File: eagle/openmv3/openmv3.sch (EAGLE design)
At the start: 56 parts, among them Q1 MOSFET, U1 STM32F765VGT6, U2 OV7725, U3 BD33IA, X1 47571-0001

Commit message: Added 3 more I/O pins
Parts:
- added R4: 100K, sfe:RESISTOR0603-RES
- JP3: device pinhead:PINHD-1X5 -> SparkFun-Connectors:M06SILK_FEMALE_PTH
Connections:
- net N$1 renamed VREFH
- net N$10 renamed LED_IR_4
- net N$12 renamed VDDA
- net N$13 renamed AVDD
- net N$14 renamed LED_IR_3
- net N$15 renamed DVDD
- net N$17 renamed LED_IR_5
- net N$2 renamed OSC_OUT
- net N$3 renamed VREFN
- net N$4 renamed OSC_IN
- net N$5 renamed LED_IR_2
- net N$6 renamed LED_B_2
- net N$7 renamed VBUS_PRE
- net N$8 renamed LED_R_2
- net N$9 renamed LED_G_2
- removed net EXPST: U1.PD8/FSMC_D13/USART3_TX
- removed net FREX: U1.PD9/FSMC_D14/USART3_RX
- removed net TIM4_CH3: JP1.4, U1.PD14/FSMC_D0/TIM4_CH3
- new net ADC: JP1.2, U1.PA7/SPI1_MOSI/TIM8_CH1N/TIM14_CH1TIM3_CH2
- new net CAN_RX: JP1.4, U1.PB3/JTDO/TRACESWO/SPI3_SCK/I2S3_CK/TIM2_CH2/SPI1_SCK
- new net CAN_TX: JP1.3, U1.PB4/NJTRST/SPI3_MISO/TIM3_CH1/SPI1_MISO/I2S3EXT_SD
- net BOOT0: now also JP3.4; no longer JP1.2
- net FSIN: now also JP1.1, U1.PD3/FSMC_CLK/USART2_CTS; no longer JP1.3
- net GND: now also JP3.1, R4.1; no longer JP3.5
- net NRST: no longer JP1.1
- net SWCLK: now also JP3.6; no longer JP3.1
- net SWDIO: now also JP3.5; no longer JP3.2
- net VBUS: now also R4.2
- net VCC: now also JP3.2; no longer JP3.4

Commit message: Swap BOOT0 and RST pins
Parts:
- R4: value 100K -> 470K
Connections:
- net BOOT0: now also JP3.3, RN5A.2; no longer JP3.4, RN5B.2
- net GND: now also RN5A.1; no longer RN5B.1
- net NRST: now also JP3.4, RN5B.2; no longer JP3.3, RN5A.2
- net VCC: now also RN5B.1; no longer RN5A.1
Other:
- note added: "Copyright (c) 2016 Ibrahim Abd Elkader <i.abdalkader@gmail.com>"
- note removed: "Copyright (c) 2013 Ibrahim Abd Elkader <i.abdalkader@gmail.com>"
- moved on the sheet: RN5A, RN5B
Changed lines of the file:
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@@
 <part name="P+13" library="mux" deviceset="VCC" device=""/>
 <part name="JP3" library="SparkFun-Connectors" deviceset="M06" device="SILK_FEMALE_PTH"/>
-<part name="R4" library="sfe" deviceset="RESISTOR" device="0603-RES" value="100K"/>
+<part name="R4" library="sfe" deviceset="RESISTOR" device="0603-RES" value="470K"/>
 <part name="GND7" library="supply1" deviceset="GND" device=""/>
 <part name="VBUS1" library="iofault" deviceset="VBUS" device=""/>
@@
 <wire x1="-20.32" y1="-48.26" x2="-20.32" y2="335.28" width="0.1524" layer="94"/>
 <wire x1="254" y1="335.28" x2="254" y2="-48.26" width="0.1524" layer="94"/>
-<text x="-15.24" y="-30.48" size="3.81" layer="150">Copyright (c) 2013 Ibrahim Abd Elkader &lt;i.abdalkader@gmail.com&gt;</text>
+<text x="-15.24" y="-30.48" size="3.81" layer="150">Copyright (c) 2016 Ibrahim Abd Elkader &lt;i.abdalkader@gmail.com&gt;</text>
 <text x="-15.24" y="-35.56" size="3.81" layer="150">This work is licensed under the Creative Commons Attribution-ShareAlike 3.0 License.</text>
 <text x="-15.24" y="-40.64" size="3.81" layer="150">To view a copy of this license, visit http://creativecommons.org/licenses/by-sa/3.0/</text>
@@
 <attribute name="NAME" x="374.015" y="187.452" size="1.016" layer="95"/>
 </instance>
-<instance part="RN5" gate="A" x="50.8" y="205.74" smashed="yes" rot="R270">
+<instance part="RN5" gate="B" x="50.8" y="205.74" smashed="yes" rot="R270">
 <attribute name="VALUE" x="47.752" y="203.2" size="1.778" layer="96" rot="R270"/>
 <attribute name="NAME" x="50.292" y="207.645" size="1.016" layer="95" rot="R270"/>
 </instance>
-<instance part="RN5" gate="B" x="22.86" y="154.94" smashed="yes" rot="R90">
+<instance part="RN5" gate="A" x="22.86" y="154.94" smashed="yes" rot="R90">
 <attribute name="VALUE" x="25.908" y="157.48" size="1.778" layer="96" rot="R90"/>
 <attribute name="NAME" x="23.368" y="153.035" size="1.016" layer="95" rot="R90"/>
@@
 <segment>
 <pinref part="GND45" gate="1" pin="GND"/>
-<pinref part="RN5" gate="B" pin="1"/>
+<pinref part="RN5" gate="A" pin="1"/>
 <wire x1="22.86" y1="149.86" x2="22.86" y2="132.08" width="0.1524" layer="91"/>
 </segment>
@@
 <label x="53.34" y="165.1" size="1.778" layer="95"/>
 <pinref part="U1" gate="G$1" pin="NRST"/>
-<pinref part="RN5" gate="A" pin="2"/>
+<pinref part="RN5" gate="B" pin="2"/>
 <wire x1="50.8" y1="165.1" x2="50.8" y2="200.66" width="0.1524" layer="91"/>
 </segment>
 <segment>
-<label x="396.24" y="256.54" size="1.778" layer="95"/>
-<pinref part="JP3" gate="G$1" pin="3"/>
-<wire x1="396.24" y1="256.54" x2="406.4" y2="256.54" width="0.1524" layer="91"/>
+<pinref part="JP3" gate="G$1" pin="4"/>
+<wire x1="406.4" y1="259.08" x2="396.24" y2="259.08" width="0.1524" layer="91"/>
+<label x="396.24" y="259.08" size="1.778" layer="95"/>
 </segment>
 </net>
@@
 <label x="53.34" y="162.56" size="1.778" layer="95"/>
 <pinref part="U1" gate="G$1" pin="BOOT0"/>
-<pinref part="RN5" gate="B" pin="2"/>
+<pinref part="RN5" gate="A" pin="2"/>
 <wire x1="22.86" y1="162.56" x2="22.86" y2="160.02" width="0.1524" layer="91"/>
 </segment>
 <segment>
-<pinref part="JP3" gate="G$1" pin="4"/>
-<wire x1="406.4" y1="259.08" x2="396.24" y2="259.08" width="0.1524" layer="91"/>
-<label x="396.24" y="259.08" size="1.778" layer="95"/>
+<pinref part="JP3" gate="G$1" pin="3"/>
+<wire x1="406.4" y1="256.54" x2="396.24" y2="256.54" width="0.1524" layer="91"/>
+<label x="396.24" y="256.54" size="1.778" layer="95"/>
 </segment>
 </net>
@@
 <segment>
 <pinref part="P+2" gate="VCC" pin="VCC"/>
-<pinref part="RN5" gate="A" pin="1"/>
+<pinref part="RN5" gate="B" pin="1"/>
 <wire x1="50.8" y1="210.82" x2="50.8" y2="220.98" width="0.1524" layer="91"/>
 </segment>

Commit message: Update OpenMV3 design files.
* Fix silk screen.
* Fix power diode part number.
* Replace IR LEDs.
* Revert last two commits.
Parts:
- removed R4: 470K, sfe:RESISTOR0603-RES
- D1: value BAT54C -> PMEG2005CT
- JP3: device SparkFun-Connectors:M06SILK_FEMALE_PTH -> pinhead:PINHD-1X5
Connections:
- net AVDD renamed N$13
- net DVDD renamed N$15
- net LED_B_2 renamed N$6
- net LED_G_2 renamed N$9
- net LED_IR_2 renamed N$5
- net LED_IR_3 renamed N$14
- net LED_IR_4 renamed N$10
- net LED_IR_5 renamed N$17
- net LED_R_2 renamed N$8
- net OSC_IN renamed N$4
- net OSC_OUT renamed N$2
- net VBUS_PRE renamed N$7
- net VDDA renamed N$12
- net VREFH renamed N$1
- net VREFN renamed N$3
- removed net ADC: JP1.2, U1.PA7/SPI1_MOSI/TIM8_CH1N/TIM14_CH1TIM3_CH2
- removed net CAN_RX: JP1.4, U1.PB3/JTDO/TRACESWO/SPI3_SCK/I2S3_CK/TIM2_CH2/SPI1_SCK
- removed net CAN_TX: JP1.3, U1.PB4/NJTRST/SPI3_MISO/TIM3_CH1/SPI1_MISO/I2S3EXT_SD
- new net EXPST: U1.PD8/FSMC_D13/USART3_TX
- new net FREX: U1.PD9/FSMC_D14/USART3_RX
- new net TIM4_CH3: JP1.4, U1.PD14/FSMC_D0/TIM4_CH3
- net BOOT0: now also JP1.2, RN5B.2; no longer JP3.3, RN5A.2
- net FSIN: now also JP1.3; no longer JP1.1, U1.PD3/FSMC_CLK/USART2_CTS
- net GND: now also JP3.5, RN5B.1; no longer JP3.1, R4.1, RN5A.1
- net NRST: now also JP1.1, JP3.3, RN5A.2; no longer JP3.4, RN5B.2
- net SWCLK: now also JP3.1; no longer JP3.6
- net SWDIO: now also JP3.2; no longer JP3.5
- net VBUS: no longer R4.2
- net VCC: now also JP3.4, RN5A.1; no longer JP3.2, RN5B.1
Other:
- note added: "Copyright (c) 2013 Ibrahim Abd Elkader <i.abdalkader@gmail.com>"
- note removed: "Copyright (c) 2016 Ibrahim Abd Elkader <i.abdalkader@gmail.com>"
- moved on the sheet: RN5A, RN5B

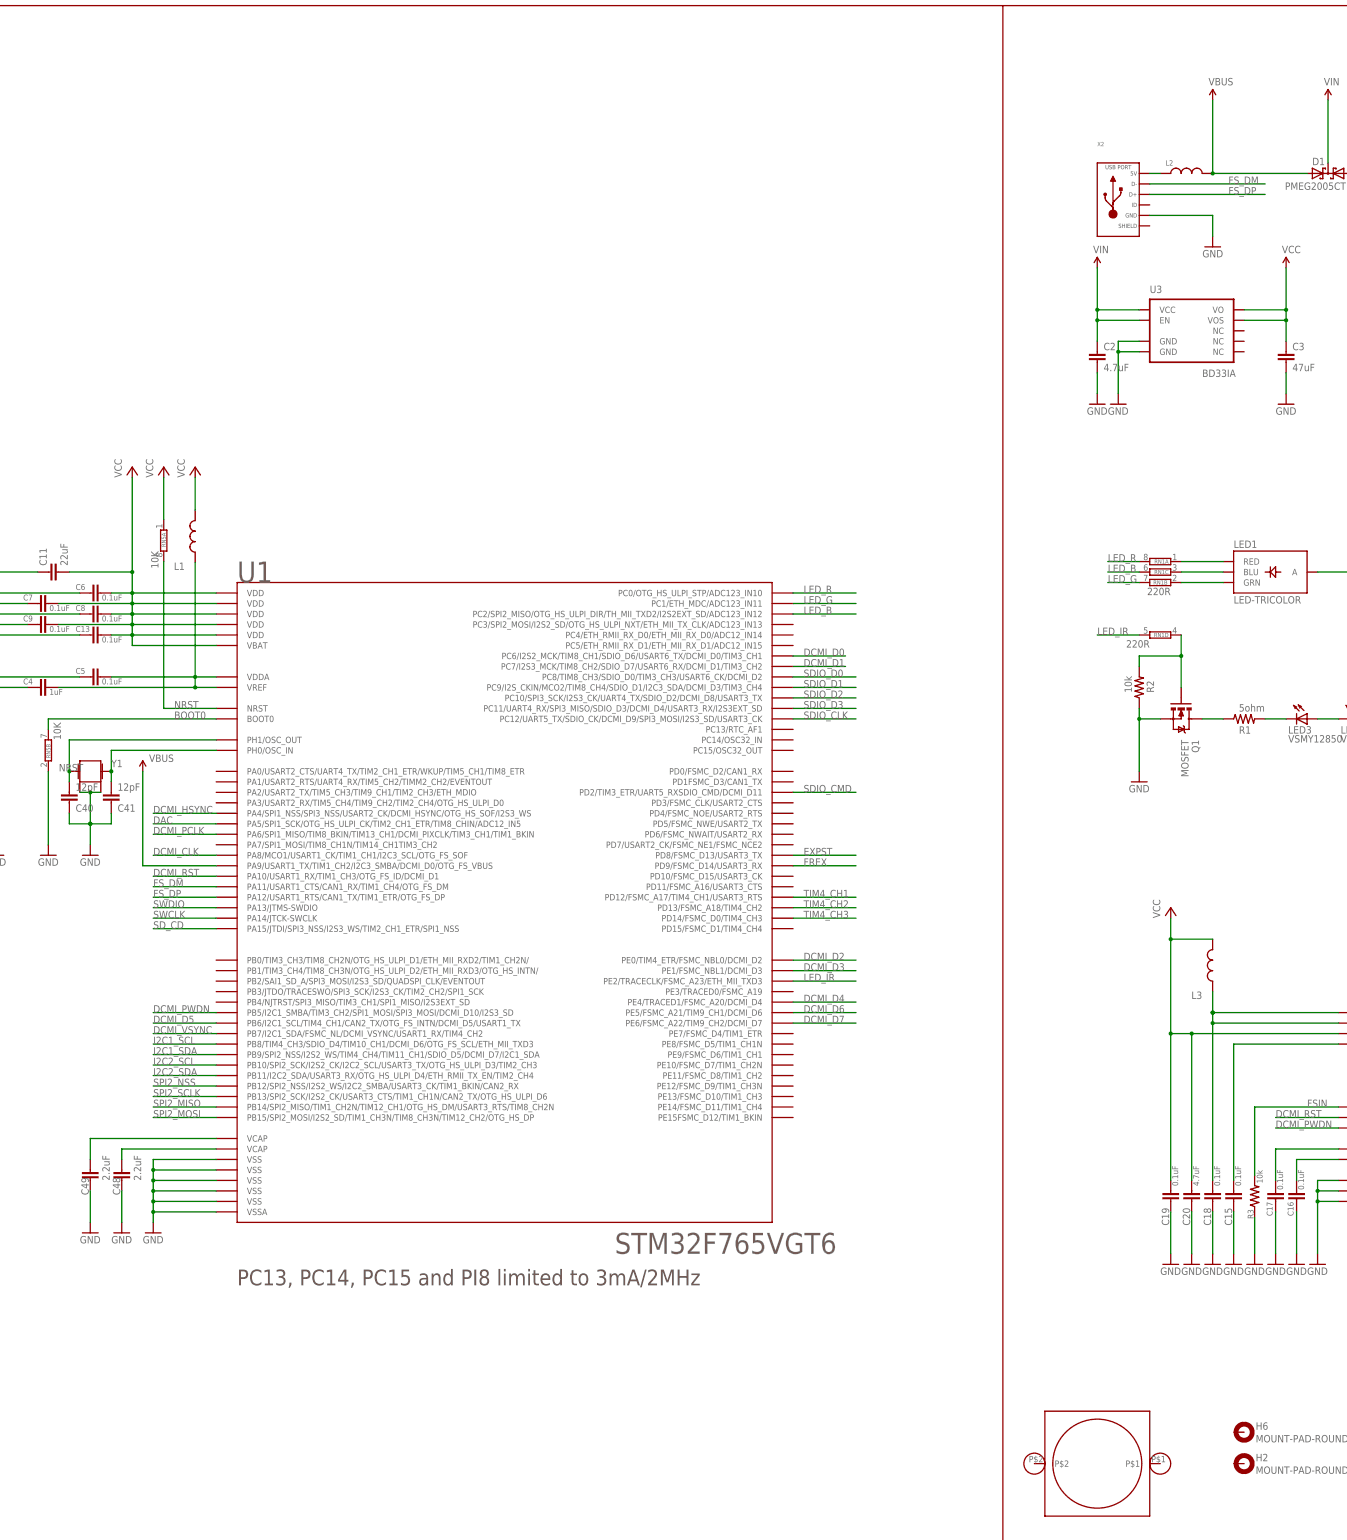
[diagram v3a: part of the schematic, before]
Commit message: Add missing parts values to OMV3 design files.
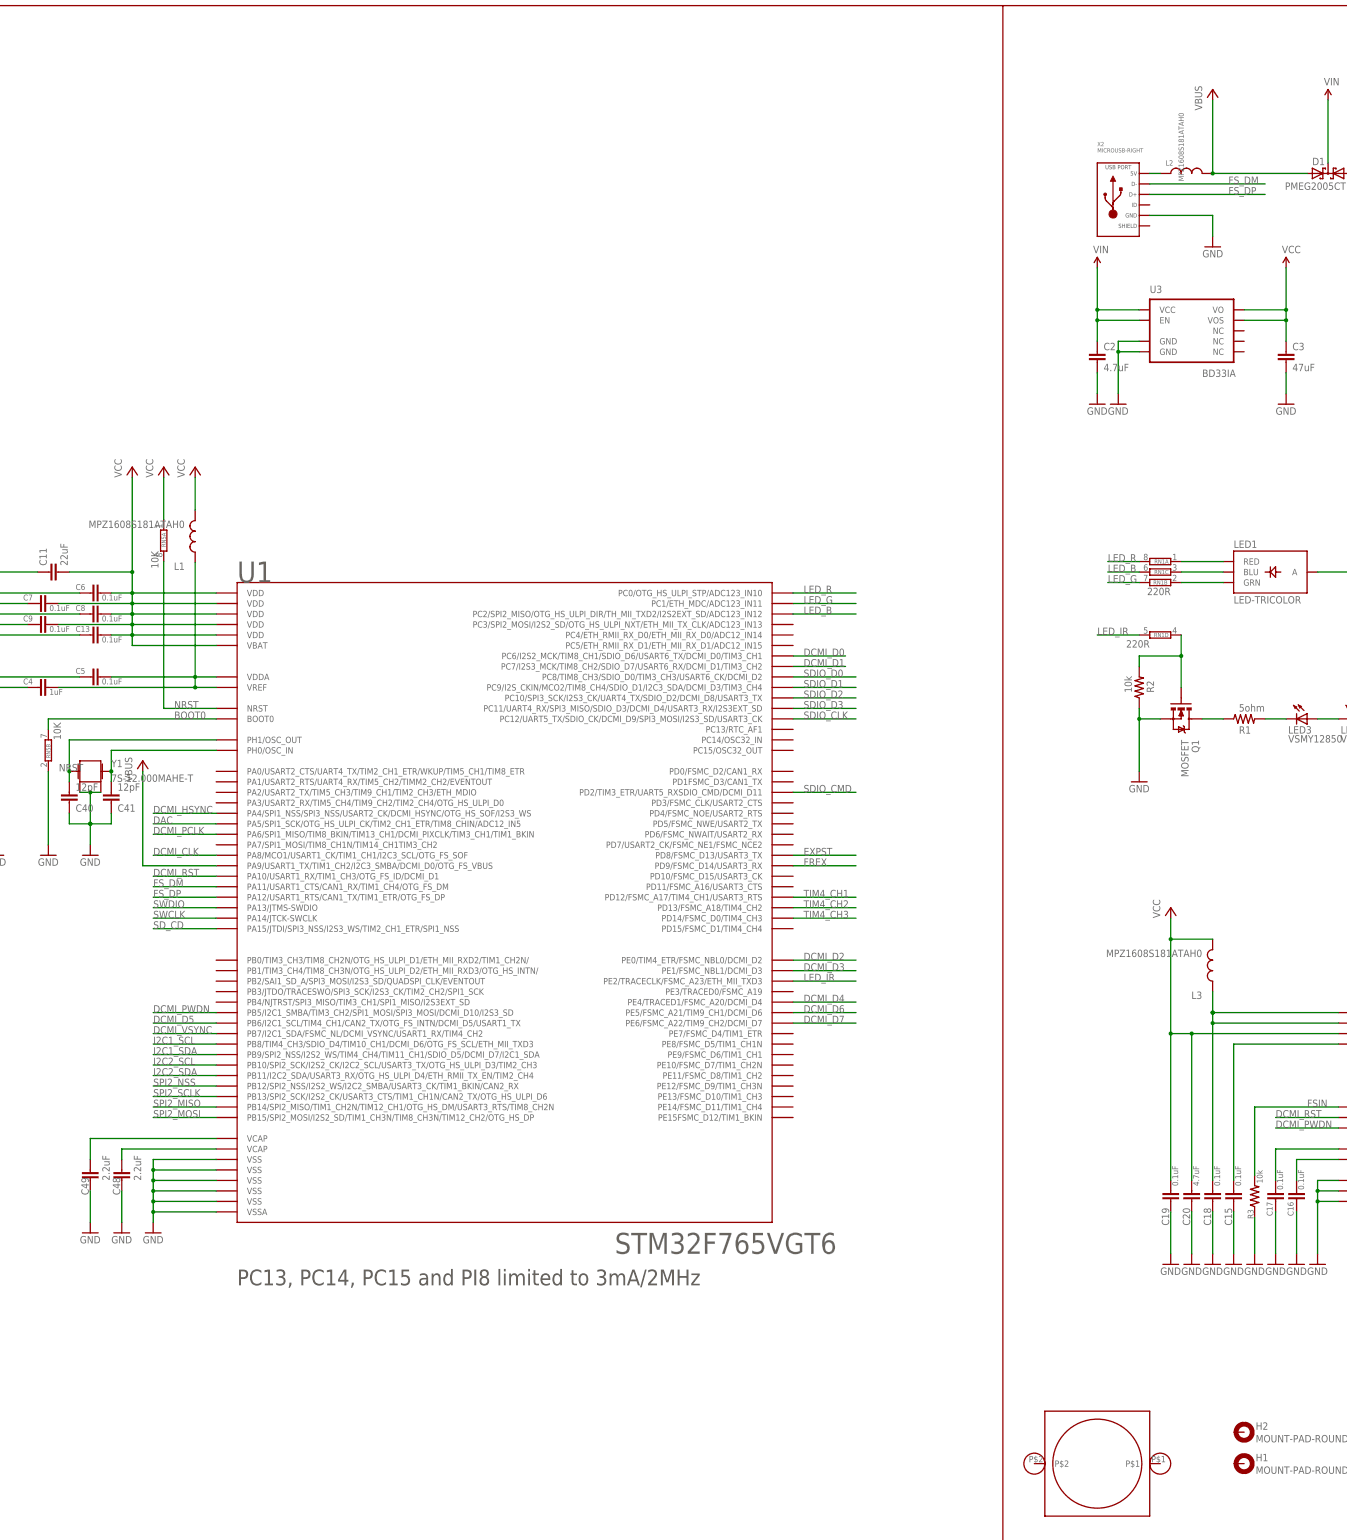
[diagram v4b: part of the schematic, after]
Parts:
- removed H6: MOUNT-PAD-ROUND2.8, holes:MOUNT-PAD-ROUND2.8
- added H1: MOUNT-PAD-ROUND2.8, holes:MOUNT-PAD-ROUND2.8
- L1, L2, L3: value (none) -> MPZ1608S181ATAH0
- X2: value (none) -> MICROUSB-RIGHT
- Y1: value (none) -> 7S-12.000MAHE-T
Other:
- moved on the sheet: H2
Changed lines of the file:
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@@
 </classes>
 <parts>
-<part name="H6" library="holes" deviceset="MOUNT-PAD-ROUND" device="2.8"/>
+<part name="H2" library="holes" deviceset="MOUNT-PAD-ROUND" device="2.8"/>
 <part name="GND16" library="sfe" deviceset="GND" device=""/>
 <part name="C40" library="sfe" deviceset="CAP" device="0603-CAP" value="12pF"/>
@@
 <part name="GND17" library="SparkFun" deviceset="GND" device=""/>
 <part name="GND19" library="SparkFun" deviceset="GND" device=""/>
-<part name="L3" library="sfe" deviceset="INDUCTOR" device="0603"/>
+<part name="L3" library="sfe" deviceset="INDUCTOR" device="0603" value="MPZ1608S181ATAH0"/>
 <part name="C19" library="sfe" deviceset="CAP" device="0603-CAP" value="0.1uF"/>
 <part name="C20" library="sfe" deviceset="CAP" device="0603-CAP" value="4.7uF"/>
@@
 <part name="GND13" library="SparkFun" deviceset="GND" device=""/>
 <part name="LM1" library="omnivision" deviceset="LENSMOUNT" device="20MM"/>
-<part name="H2" library="holes" deviceset="MOUNT-PAD-ROUND" device="2.8"/>
+<part name="H1" library="holes" deviceset="MOUNT-PAD-ROUND" device="2.8"/>
 <part name="GND10" library="supply1" deviceset="GND" device=""/>
 <part name="P+5" library="supply1" deviceset="VCC" device=""/>
@@
 <attribute name="OC_NEWARK" value="unknown"/>
 </part>
-<part name="L1" library="sfe" deviceset="INDUCTOR" device="0603"/>
+<part name="L1" library="sfe" deviceset="INDUCTOR" device="0603" value="MPZ1608S181ATAH0"/>
 <part name="P+8" library="supply1" deviceset="VCC" device=""/>
 <part name="C15" library="sfe" deviceset="CAP" device="0603-CAP" value="0.1uF"/>
@@
 <part name="LED1" library="sfe" deviceset="LED-TRICOLOR" device="" value="LED-TRICOLOR"/>
 <part name="P+11" library="SparkFun" deviceset="VCC" device=""/>
-<part name="Y1" library="mux" deviceset="CRYSTAL" device="2.5X2.0"/>
+<part name="Y1" library="mux" deviceset="CRYSTAL" device="2.5X2.0" value="7S-12.000MAHE-T"/>
 <part name="LOGO1" library="iofault" deviceset="OSHW_LOGO_FILL" device="X0100-NT"/>
 <part name="FRAME1" library="frames" deviceset="DINA3_L" device=""/>
@@
 <part name="GND42" library="sfe" deviceset="GND" device=""/>
 <part name="GND45" library="sfe" deviceset="GND" device=""/>
-<part name="U$8" library="mux" deviceset="VBUS" device=""/>
 <part name="JP1" library="pinhead" deviceset="PINHD-1X8" device=""/>
 <part name="JP2" library="pinhead" deviceset="PINHD-1X8" device=""/>
 <part name="GND3" library="sfe" deviceset="GND" device=""/>
-<part name="L2" library="sfe" deviceset="INDUCTOR" device="0603"/>
+<part name="L2" library="sfe" deviceset="INDUCTOR" device="0603" value="MPZ1608S181ATAH0"/>
 <part name="P+7" library="iofault" deviceset="VIN" device=""/>
 <part name="C1" library="sfe" deviceset="CAP" device="0805" value="22uF"/>
@@
 <part name="P+4" library="supply1" deviceset="VCC" device=""/>
 <part name="U2" library="omnivision" deviceset="OV7725" device=""/>
-<part name="VBUS" library="iofault" deviceset="VBUS" device=""/>
 <part name="U1" library="stm32" deviceset="STM32F746" device="LQFP100" value="STM32F765VGT6"/>
 <part name="P+12" library="SparkFun" deviceset="VCC" device=""/>
-<part name="X2" library="MF_Connectors" deviceset="USB" device="_MICRO_RIGHT"/>
+<part name="X2" library="MF_Connectors" deviceset="USB" device="_MICRO_RIGHT" value="MICROUSB-RIGHT"/>
 <part name="JP3" library="pinhead" deviceset="PINHD-1X5" device=""/>
 <part name="GND22" library="SparkFun" deviceset="GND" device=""/>
@@
 <part name="LED3" library="sfe" deviceset="LED" device="1206" value="VSMY12850"/>
 <part name="P+13" library="mux" deviceset="VCC" device=""/>
+<part name="VBUS2" library="supply" deviceset="VBUS" device=""/>
+<part name="VBUS1" library="supply" deviceset="VBUS" device=""/>
 </parts>
 <sheets>
@@
 </plain>
 <instances>
-<instance part="H6" gate="G$1" x="312.42" y="-10.16"/>
+<instance part="H2" gate="G$1" x="312.42" y="-10.16"/>
 <instance part="GND16" gate="1" x="33.02" y="129.54"/>
 <instance part="C40" gate="G$1" x="27.94" y="144.78" rot="MR180"/>
@@
 <instance part="GND13" gate="1" x="360.68" y="152.4" rot="MR0"/>
 <instance part="LM1" gate="G$1" x="276.86" y="-17.78" rot="R180"/>
-<instance part="H2" gate="G$1" x="312.42" y="-17.78"/>
+<instance part="H1" gate="G$1" x="312.42" y="-17.78"/>
 <instance part="GND10" gate="1" x="322.58" y="238.76"/>
 <instance part="P+5" gate="VCC" x="414.02" y="109.22"/>
@@
 <instance part="GND42" gate="1" x="33.02" y="38.1"/>
 <instance part="GND45" gate="1" x="22.86" y="129.54"/>
-<instance part="U$8" gate="G$1" x="45.72" y="149.86" smashed="yes" rot="MR0">
-<attribute name="VALUE" x="47.244" y="153.924" size="1.778" layer="96" rot="MR180"/>
-</instance>
 <instance part="JP1" gate="A" x="370.84" y="299.72"/>
 <instance part="JP2" gate="A" x="416.56" y="299.72"/>
@@
 <instance part="P+4" gate="VCC" x="294.64" y="116.84"/>
 <instance part="U2" gate="G$1" x="358.14" y="63.5"/>
-<instance part="VBUS" gate="G$1" x="304.8" y="312.42"/>
 <instance part="U1" gate="G$1" x="129.54" y="119.38" smashed="yes">
 <attribute name="NAME" x="68.58" y="195.58" size="5.08" layer="95" ratio="16"/>
@@
 <instance part="LED3" gate="G$1" x="327.66" y="162.56" rot="R270"/>
 <instance part="P+13" gate="1" x="391.16" y="274.32"/>
+<instance part="VBUS2" gate="G$1" x="45.72" y="149.86"/>
+<instance part="VBUS1" gate="G$1" x="304.8" y="312.42"/>
 </instances>
 <busses>
@@
 <net name="VBUS" class="0">
 <segment>
-<pinref part="U$8" gate="G$1" pin="VBUS"/>
 <wire x1="63.5" y1="127" x2="45.72" y2="127" width="0.1524" layer="91"/>
 <wire x1="45.72" y1="127" x2="45.72" y2="149.86" width="0.1524" layer="91"/>
 <pinref part="U1" gate="G$1" pin="PA9/USART1_TX/TIM1_CH2/I2C3_SMBA/DCMI_D0/OTG_FS_VBUS"/>
+<pinref part="VBUS2" gate="G$1" pin="VBUS"/>
 </segment>
 <segment>
@@
 <junction x="304.8" y="294.64"/>
 <pinref part="D1" gate="G$1" pin="A2"/>
-<pinref part="VBUS" gate="G$1" pin="VBUS"/>
+<pinref part="VBUS1" gate="G$1" pin="VBUS"/>
 </segment>
 </net>
